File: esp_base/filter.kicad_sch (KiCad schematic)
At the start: 3 parts

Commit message: NEW PADS
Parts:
- I1: footprint TestPoint:TestPoint_THTPad_D2.0mm_Drill1.0mm -> TestPoint:TestPoint_Pad_2.0x2.0mm
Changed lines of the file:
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@@
+	)
+	(symbol
+		(lib_id "Device:C")
+		(at 121.92 83.82 0)
+		(unit 1)
+		(exclude_from_sim no)
+		(in_bom yes)
+		(on_board yes)
+		(dnp no)
+		(property "Reference" "C4"
+			(at 125.73 82.5499 0)
+			(effects
+				(font
+					(size 1.27 1.27)
+				)
+				(justify left)
+			)
+		)
+		(property "Value" "4u7"
+			(at 125.73 85.0899 0)
+			(effects
+				(font
+					(size 1.27 1.27)
+				)
+				(justify left)
+			)
+		)
+		(property "Footprint" "Capacitor_SMD:C_0805_2012Metric"
+			(at 122.8852 87.63 0)
+			(effects
+				(font
+					(size 1.27 1.27)
+				)
+				(hide yes)
+			)
+		)
+		(property "Datasheet" "~"
+			(at 121.92 83.82 0)
+			(effects
+				(font
+					(size 1.27 1.27)
+				)
+				(hide yes)
+			)
+		)
+		(property "Description" "Unpolarized capacitor"
+			(at 121.92 83.82 0)
+			(effects
+				(font
+					(size 1.27 1.27)
+				)
+				(hide yes)
+			)
+		)
+		(pin "1"
+		)
+		(pin "2"
+		)
+		(instances
+			(project "esp_base"
+				(path "/b9883b8e-181f-47a1-bc04-7eade380b6a1/01f32a3b-3855-4b75-a03c-490b035f36f1"
+					(reference "C4")
+					(unit 1)
+				)
+				(path "/b9883b8e-181f-47a1-bc04-7eade380b6a1/18575c04-1730-46c3-ae87-a1b5af41a75f"
+					(reference "C12")
+					(unit 1)
+				)
+				(path "/b9883b8e-181f-47a1-bc04-7eade380b6a1/2462927e-59f4-4eec-8d96-fcf1833190f0"
+					(reference "C13")
+					(unit 1)
+				)
+				(path "/b9883b8e-181f-47a1-bc04-7eade380b6a1/27795937-c523-476e-a3eb-72f0355cd2da"
+					(reference "C18")
+					(unit 1)
+				)
+				(path "/b9883b8e-181f-47a1-bc04-7eade380b6a1/389f97b2-e30d-4847-bdcb-d0940d09a33f"
+					(reference "C16")
+					(unit 1)
+				)
+				(path "/b9883b8e-181f-47a1-bc04-7eade380b6a1/3d1ee391-c52c-4d0a-9dac-e5b5117b5824"
+					(reference "C9")
+					(unit 1)
+				)
+				(path "/b9883b8e-181f-47a1-bc04-7eade380b6a1/443ad700-5db0-4a57-9967-b9ab88f2acf0"
+					(reference "C14")
+					(unit 1)
+				)
+				(path "/b9883b8e-181f-47a1-bc04-7eade380b6a1/56a5e6ef-5569-4e28-baba-bf73d0a17f07"
+					(reference "C11")
+					(unit 1)
+				)
+				(path "/b9883b8e-181f-47a1-bc04-7eade380b6a1/a7235410-2217-4115-a8f5-356c2a37b83f"
+					(reference "C8")
+					(unit 1)
+				)
+				(path "/b9883b8e-181f-47a1-bc04-7eade380b6a1/aa90cb4d-9d66-4e69-850d-355f51c51508"
+					(reference "C10")
+					(unit 1)
+				)
+				(path "/b9883b8e-181f-47a1-bc04-7eade380b6a1/c6dfab4f-5a96-4386-9fa3-e917acdbb7a6"
+					(reference "C15")
+					(unit 1)
+				)
+				(path "/b9883b8e-181f-47a1-bc04-7eade380b6a1/e7e8cab3-f61b-47c5-8a05-d522324e1d5d"
+					(reference "C17")
+					(unit 1)
+				)
+			)
+		)
 	)
 	(symbol
@@
 		(fields_autoplaced yes)
 		(property "Reference" "I1"
-			(at 139.7 74.1679 0)
+			(at 139.7 75.4379 0)
 			(effects
 				(font
@@
 				)
 				(justify left)
-			)
-		)
-		(property "Footprint" "TestPoint:TestPoint_THTPad_D2.0mm_Drill1.0mm"
+				(hide yes)
+			)
+		)
+		(property "Footprint" "TestPoint:TestPoint_Pad_2.0x2.0mm"
 			(at 142.24 78.74 0)
 			(effects
@@
 					(unit 1)
 				)
-			)
-		)
-	)
-	(symbol
-		(lib_id "Device:C")
-		(at 121.92 83.82 0)
-		(unit 1)
-		(exclude_from_sim no)
-		(in_bom yes)
-		(on_board yes)
-		(dnp no)
-		(property "Reference" "C4"
-			(at 125.73 82.5499 0)
-			(effects
-				(font
-					(size 1.27 1.27)
-				)
-				(justify left)
-			)
-		)
-		(property "Value" "4u7"
-			(at 125.73 85.0899 0)
-			(effects
-				(font
-					(size 1.27 1.27)
-				)
-				(justify left)
-			)
-		)
-		(property "Footprint" "Capacitor_SMD:C_0805_2012Metric"
-			(at 122.8852 87.63 0)
-			(effects
-				(font
-					(size 1.27 1.27)
-				)
-				(hide yes)
-			)
-		)
-		(property "Datasheet" "~"
-			(at 121.92 83.82 0)
-			(effects
-				(font
-					(size 1.27 1.27)
-				)
-				(hide yes)
-			)
-		)
-		(property "Description" "Unpolarized capacitor"
-			(at 121.92 83.82 0)
-			(effects
-				(font
-					(size 1.27 1.27)
-				)
-				(hide yes)
-			)
-		)
-		(pin "1"
-		)
-		(pin "2"
-		)
-		(instances
-			(project "esp_base"
-				(path "/b9883b8e-181f-47a1-bc04-7eade380b6a1/01f32a3b-3855-4b75-a03c-490b035f36f1"
-					(reference "C4")
-					(unit 1)
-				)
-				(path "/b9883b8e-181f-47a1-bc04-7eade380b6a1/18575c04-1730-46c3-ae87-a1b5af41a75f"
-					(reference "C12")
-					(unit 1)
-				)
-				(path "/b9883b8e-181f-47a1-bc04-7eade380b6a1/2462927e-59f4-4eec-8d96-fcf1833190f0"
-					(reference "C13")
-					(unit 1)
-				)
-				(path "/b9883b8e-181f-47a1-bc04-7eade380b6a1/27795937-c523-476e-a3eb-72f0355cd2da"
-					(reference "C18")
-					(unit 1)
-				)
-				(path "/b9883b8e-181f-47a1-bc04-7eade380b6a1/389f97b2-e30d-4847-bdcb-d0940d09a33f"
-					(reference "C16")
-					(unit 1)
-				)
-				(path "/b9883b8e-181f-47a1-bc04-7eade380b6a1/3d1ee391-c52c-4d0a-9dac-e5b5117b5824"
-					(reference "C9")
-					(unit 1)
-				)
-				(path "/b9883b8e-181f-47a1-bc04-7eade380b6a1/443ad700-5db0-4a57-9967-b9ab88f2acf0"
-					(reference "C14")
-					(unit 1)
-				)
-				(path "/b9883b8e-181f-47a1-bc04-7eade380b6a1/56a5e6ef-5569-4e28-baba-bf73d0a17f07"
-					(reference "C11")
-					(unit 1)
-				)
-				(path "/b9883b8e-181f-47a1-bc04-7eade380b6a1/a7235410-2217-4115-a8f5-356c2a37b83f"
-					(reference "C8")
-					(unit 1)
-				)
-				(path "/b9883b8e-181f-47a1-bc04-7eade380b6a1/aa90cb4d-9d66-4e69-850d-355f51c51508"
-					(reference "C10")
-					(unit 1)
-				)
-				(path "/b9883b8e-181f-47a1-bc04-7eade380b6a1/c6dfab4f-5a96-4386-9fa3-e917acdbb7a6"
-					(reference "C15")
-					(unit 1)
-				)
-				(path "/b9883b8e-181f-47a1-bc04-7eade380b6a1/e7e8cab3-f61b-47c5-8a05-d522324e1d5d"
-					(reference "C17")
-					(unit 1)
-				)

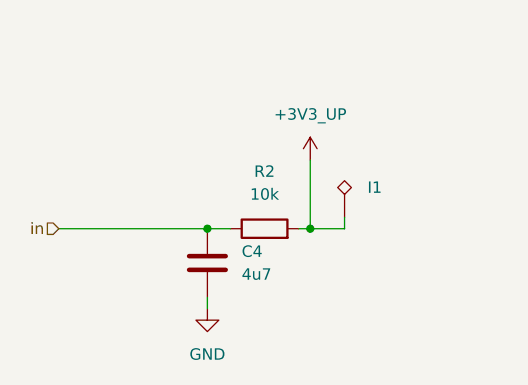
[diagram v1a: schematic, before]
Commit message: last version with cahges on pull up resistor
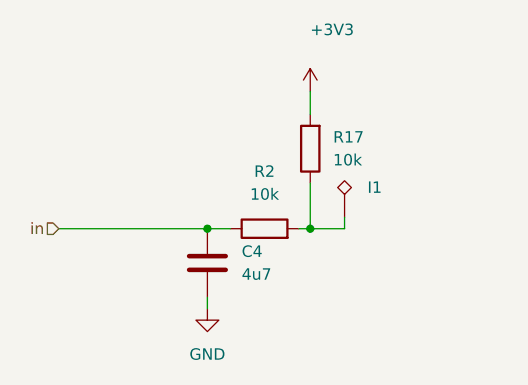
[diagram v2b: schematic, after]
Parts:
- added R17: 10k, Resistor_SMD:R_0805_2012Metric, symbol Device:R
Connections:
- net +3V3_UP: no longer names the net of I1.1, R2.2
- net +3V3_UP: now also R17.1
- new net +3V3: R17.2
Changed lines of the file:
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@@
 	(wire
 		(pts
-			(xy 133.35 72.39) (xy 133.35 80.01)
+			(xy 133.35 80.01) (xy 137.16 80.01)
+		)
+		(stroke
+			(width 0)
+			(type default)
+		)
+	)
+	(wire
+		(pts
+			(xy 133.35 74.93) (xy 133.35 80.01)
+		)
+		(stroke
+			(width 0)
+			(type default)
+		)
+	)
+	(wire
+		(pts
+			(xy 137.16 78.74) (xy 137.16 80.01)
+		)
+		(stroke
+			(width 0)
+			(type default)
+		)
+	)
+	(wire
+		(pts
+			(xy 121.92 80.01) (xy 124.46 80.01)
 		)
 		(stroke
@@
 	(wire
 		(pts
-			(xy 137.16 78.74) (xy 137.16 80.01)
-		)
-		(stroke
-			(width 0)
-			(type default)
-		)
-	)
-	(wire
-		(pts
-			(xy 121.92 80.01) (xy 124.46 80.01)
-		)
-		(stroke
-			(width 0)
-			(type default)
-		)
-	)
-	(wire
-		(pts
-			(xy 133.35 80.01) (xy 137.16 80.01)
-		)
-		(stroke
-			(width 0)
-			(type default)
-		)
-	)
-	(wire
-		(pts
 			(xy 121.92 87.63) (xy 121.92 88.9)
+		)
+		(stroke
+			(width 0)
+			(type default)
+		)
+	)
+	(wire
+		(pts
+			(xy 133.35 64.77) (xy 133.35 67.31)
 		)
 		(stroke
@@
 	)
 	(symbol
+		(lib_id "Device:R")
+		(at 133.35 71.12 180)
+		(unit 1)
+		(exclude_from_sim no)
+		(in_bom yes)
+		(on_board yes)
+		(dnp no)
+		(fields_autoplaced yes)
+		(property "Reference" "R17"
+			(at 135.89 69.8499 0)
+			(effects
+				(font
+					(size 1.27 1.27)
+				)
+				(justify right)
+			)
+		)
+		(property "Value" "10k"
+			(at 135.89 72.3899 0)
+			(effects
+				(font
+					(size 1.27 1.27)
+				)
+				(justify right)
+			)
+		)
+		(property "Footprint" "Resistor_SMD:R_0805_2012Metric"
+			(at 135.128 71.12 90)
+			(effects
+				(font
+					(size 1.27 1.27)
+				)
+				(hide yes)
+			)
+		)
+		(property "Datasheet" "~"
+			(at 133.35 71.12 0)
+			(effects
+				(font
+					(size 1.27 1.27)
+				)
+				(hide yes)
+			)
+		)
+		(property "Description" "Resistor"
+			(at 133.35 71.12 0)
+			(effects
+				(font
+					(size 1.27 1.27)
+				)
+				(hide yes)
+			)
+		)
+		(pin "1"
+		)
+		(pin "2"
+		)
+		(instances
+			(project "esp_base"
+				(path "/b9883b8e-181f-47a1-bc04-7eade380b6a1/01f32a3b-3855-4b75-a03c-490b035f36f1"
+					(reference "R17")
+					(unit 1)
+				)
+				(path "/b9883b8e-181f-47a1-bc04-7eade380b6a1/18575c04-1730-46c3-ae87-a1b5af41a75f"
+					(reference "R22")
+					(unit 1)
+				)
+				(path "/b9883b8e-181f-47a1-bc04-7eade380b6a1/2462927e-59f4-4eec-8d96-fcf1833190f0"
+					(reference "R23")
+					(unit 1)
+				)
+				(path "/b9883b8e-181f-47a1-bc04-7eade380b6a1/27795937-c523-476e-a3eb-72f0355cd2da"
+					(reference "R28")
+					(unit 1)
+				)
+				(path "/b9883b8e-181f-47a1-bc04-7eade380b6a1/389f97b2-e30d-4847-bdcb-d0940d09a33f"
+					(reference "R26")
+					(unit 1)
+				)
+				(path "/b9883b8e-181f-47a1-bc04-7eade380b6a1/3d1ee391-c52c-4d0a-9dac-e5b5117b5824"
+					(reference "R19")
+					(unit 1)
+				)
+				(path "/b9883b8e-181f-47a1-bc04-7eade380b6a1/443ad700-5db0-4a57-9967-b9ab88f2acf0"
+					(reference "R24")
+					(unit 1)
+				)
+				(path "/b9883b8e-181f-47a1-bc04-7eade380b6a1/56a5e6ef-5569-4e28-baba-bf73d0a17f07"
+					(reference "R21")
+					(unit 1)
+				)
+				(path "/b9883b8e-181f-47a1-bc04-7eade380b6a1/a7235410-2217-4115-a8f5-356c2a37b83f"
+					(reference "R18")
+					(unit 1)
+				)
+				(path "/b9883b8e-181f-47a1-bc04-7eade380b6a1/aa90cb4d-9d66-4e69-850d-355f51c51508"
+					(reference "R20")
+					(unit 1)
+				)
+				(path "/b9883b8e-181f-47a1-bc04-7eade380b6a1/c6dfab4f-5a96-4386-9fa3-e917acdbb7a6"
+					(reference "R25")
+					(unit 1)
+				)
+				(path "/b9883b8e-181f-47a1-bc04-7eade380b6a1/e7e8cab3-f61b-47c5-8a05-d522324e1d5d"
+					(reference "R27")
+					(unit 1)
+				)
+			)
+		)
+	)
+	(symbol
 		(lib_id "Device:C")
 		(at 121.92 83.82 0)
@@
 	(symbol
 		(lib_id "power:+3V3")
-		(at 133.35 72.39 0)
+		(at 133.35 64.77 0)
 		(unit 1)
 		(exclude_from_sim no)
@@
 		(on_board yes)
 		(dnp no)
-		(fields_autoplaced yes)
 		(property "Reference" "#PWR09"
-			(at 133.35 76.2 0)
-			(effects
-				(font
-					(size 1.27 1.27)
-				)
-				(hide yes)
-			)
-		)
-		(property "Value" "+3V3_UP"
-			(at 133.35 67.31 0)
-			(effects
-				(font
-					(size 1.27 1.27)
-				)
+			(at 133.35 68.58 0)
+			(effects
+				(font
+					(size 1.27 1.27)
+				)
+				(hide yes)
+			)
+		)
+		(property "Value" "+3V3"
+			(at 133.35 57.912 0)
+			(effects
+				(font
+					(size 1.27 1.27)
+				)
+				(justify left)
 			)
 		)
 		(property "Footprint" ""
-			(at 133.35 72.39 0)
+			(at 133.35 64.77 0)
 			(effects
 				(font
@@
 		)
 		(property "Datasheet" ""
-			(at 133.35 72.39 0)
+			(at 133.35 64.77 0)
 			(effects
 				(font
@@
 		)
 		(property "Description" "Power symbol creates a global label with name \"+3V3\""
-			(at 133.35 72.39 0)
-			(effects
-				(font
+			(at 133.35 64.77 0)
+			(effects
+				(font
